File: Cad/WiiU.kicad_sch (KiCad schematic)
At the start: 0 parts

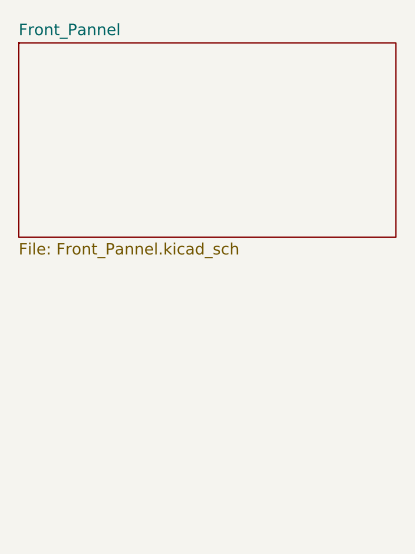
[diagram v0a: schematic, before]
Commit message: Changed the Button pannel's schematics file name to the correct name
Front_Pannel -> FRT-01
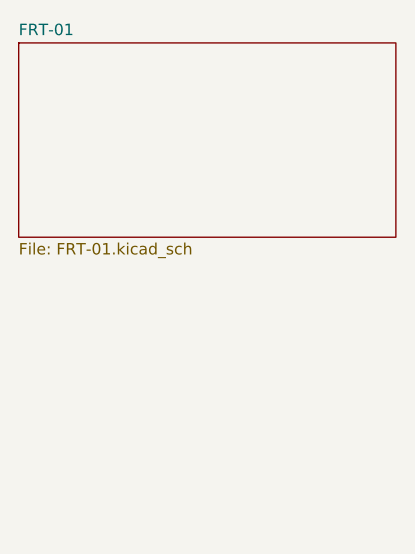
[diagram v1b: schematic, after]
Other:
- sheet Front_Pannel renamed FRT-01
- sheet FRT-01: file Front_Pannel.kicad_sch -> FRT-01.kicad_sch
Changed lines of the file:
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@@
     (stroke (width 0.1524) (type solid))
     (fill (color 0 0 0 0.0000))
-    (property "Sheetname" "Front_Pannel" (at 27.94 19.6084 0)
+    (property "Sheetname" "FRT-01" (at 27.94 19.6084 0)
       (effects (font (size 1.27 1.27)) (justify left bottom))
     )
-    (property "Sheetfile" "Front_Pannel.kicad_sch" (at 27.94 42.4946 0)
+    (property "Sheetfile" "FRT-01.kicad_sch" (at 27.94 42.4946 0)
       (effects (font (size 1.27 1.27)) (justify left top))
     )

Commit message: Added Main board schematics
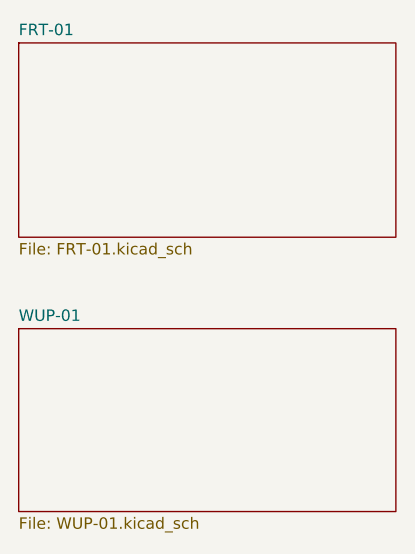
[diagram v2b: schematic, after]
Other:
- added sheet WUP-01 (WUP-01.kicad_sch)
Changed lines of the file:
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@@
+    )
+  )
+  (sheet (at 27.94 52.07) (size 41.91 20.32) (fields_autoplaced)
+    (stroke (width 0.1524) (type solid))
+    (fill (color 0 0 0 0.0000))
+    (property "Sheetname" "WUP-01" (at 27.94 51.3584 0)
+      (effects (font (size 1.27 1.27)) (justify left bottom))
+    )
+    (property "Sheetfile" "WUP-01.kicad_sch" (at 27.94 72.9746 0)
+      (effects (font (size 1.27 1.27)) (justify left top))
+    )
+    (property "Champ2" "" (at 27.94 52.07 0)
+      (effects (font (size 1.27 1.27)) hide)
+    )
+    (instances
+      (project "WiiU"
+        (path "/74046161-12f4-4e09-a474-cfaa73535c88" (page "3"))
+      )
     )
   )
